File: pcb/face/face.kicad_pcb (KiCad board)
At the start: 2 copper layers, 130 x 65 mm, 25 parts, among them J104 Conn_02x13_Counter_Clockwise, U1 K155ID1, U2 K155ID1, U3 K155ID1, U4 K155ID1

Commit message: Rev B RC1
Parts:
- removed H5: MountingHole, MountingHole:MountingHole_3.2mm_M3_ISO7380
- added H4: MountingHole, MountingHole:MountingHole_3.2mm_M3_ISO7380, F.Cu at (210.0, 120.0)
- added J2: Phoenix MSTB, Connector_Phoenix_MSTB:PhoenixContact_MSTBVA_2,5_3-G-5,08_1x03_P5.08mm_Vertical, B.Cu at (190.9, 118.3)
- J1: renamed from J104; value Conn_02x13_Counter_Clockwise -> 26 pin IDC
- moved C1 1.00 mm to (136.5, 109.0)
- moved C2 1.00 mm to (110.5, 109.0)
- moved C3 1.00 mm to (196.5, 109.0)
- moved C4 1.00 mm to (170.5, 109.0)
- moved H1 1.00 mm to (90.0, 65.0)
- moved H2 1.00 mm to (90.0, 120.0)
- moved H3 1.00 mm to (210.0, 65.0)
- moved J1 1.00 mm to (165.2, 120.0)
- moved NX1 1.00 mm to (151.0, 74.0)
- moved NX2 1.00 mm to (134.0, 79.0)
- moved NX3 1.00 mm to (108.0, 79.0)
- moved NX4 1.00 mm to (151.0, 84.0)
- moved NX5 1.00 mm to (194.0, 79.0)
- moved NX6 1.00 mm to (168.0, 79.0)
- moved R1 1.00 mm to (156.0, 66.0)
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- renumbered C2 to C1, C1 to C2, C4 to C3, C3 to C4, H2 to H1, H4 to H2, NX5 to NX1, NX1 to NX3, NX6 to NX4, NX4 to NX5, NX3 to NX6, R5 to R1, R1 to R3, R6 to R4, R4 to R5, R3 to R6, U2 to U1, U1 to U2, U4 to U3, U3 to U4
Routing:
- net GND: track 0.00 -> 135.3 mm
- net +5V: track 138.5 -> 121.9 mm
- net /NX3_{8}: track 48.6 -> 43.2 mm
- net +170V: track 304.5 -> 306.7 mm
- net M1_{B}: track 42.6 -> 41.3 mm

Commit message: Final Rev B
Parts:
- added REF**: Symbol_HighVoltage_Triangle_8x7mm_SilkScreen, nixie_clock:Symbol_HighVoltage_Triangle_8x7mm_SilkScreen, F.Cu at (182.0, 119.0)
- added REF**: Symbol_HighVoltage_Triangle_8x7mm_SilkScreen, nixie_clock:Symbol_HighVoltage_Triangle_8x7mm_SilkScreen, B.Cu at (182.0, 119.0)
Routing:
- net GND: track 135.3 -> 0.00 mm

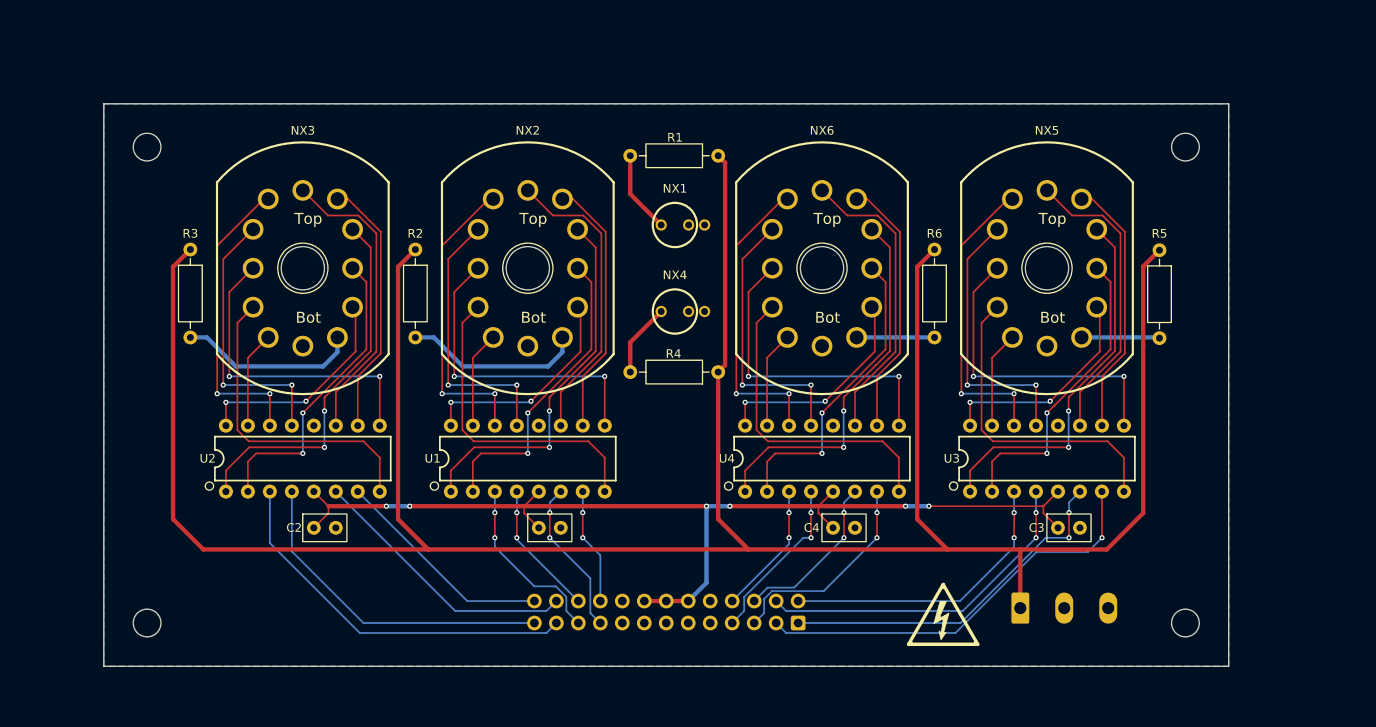
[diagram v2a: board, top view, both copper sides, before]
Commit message: HV converter Rev C redesign around LM5156
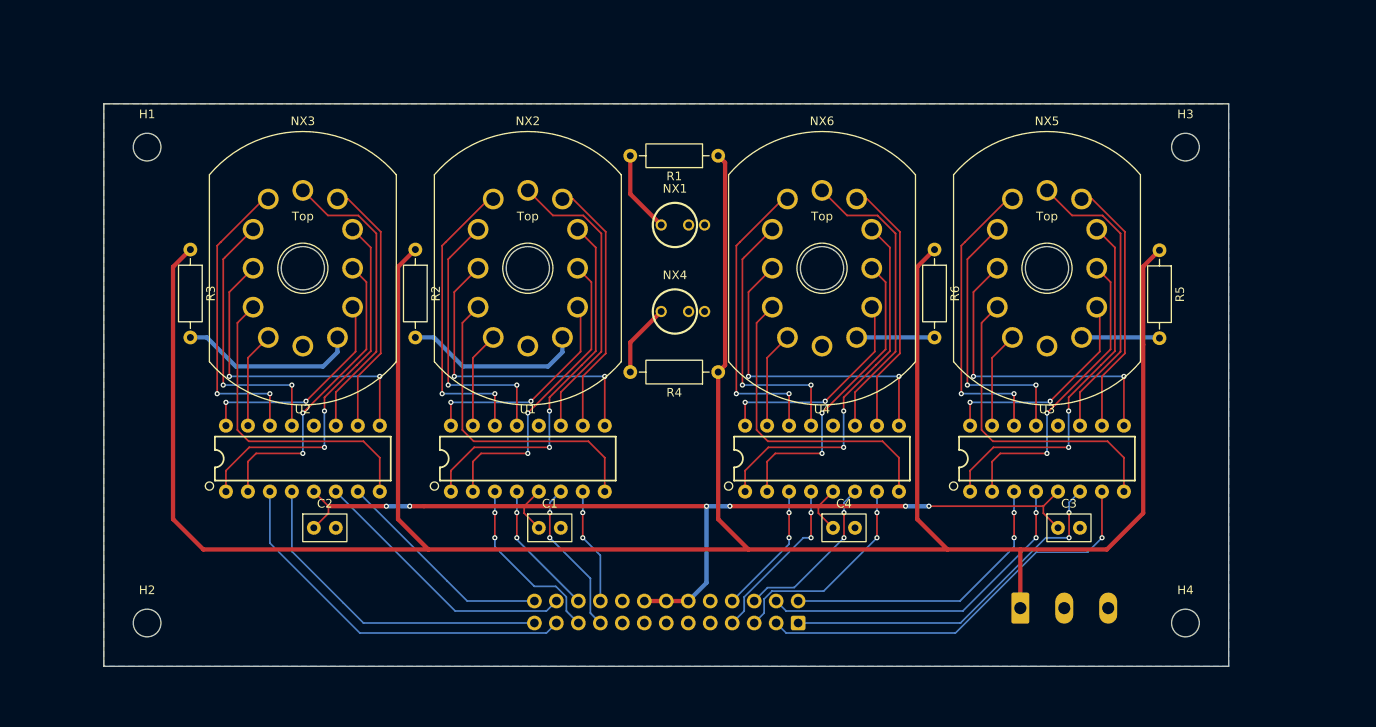
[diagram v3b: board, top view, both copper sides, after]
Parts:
- removed the REF** at (182.0, 119.0) (x2)
- added REF**: Symbol_HighVoltage_Triangle_8x7mm_CopperArrow, 0_nixie_clock:Symbol_HighVoltage_Triangle_8x7mm_CopperArrow, B.Cu at (179.5, 113.5)
- C1, C2, C3, C4: footprint nixie_clock:C_Rect_L5.1mm_W3.2mm_P2.54mm_Goldmax -> 0_nixie_clock:C_Rect_L5.1mm_W3.2mm_P2.54mm_Goldmax
- NX1, NX4: footprint nixie_clock:IN-6 -> 0_nixie_clock:IN-6
- NX2, NX3, NX5, NX6: footprint nixie_clock:IN-12-DSUB -> 0_nixie_clock:IN-12-DSUB
- U1, U2, U3, U4: footprint nixie_clock:DIP16 -> 0_nixie_clock:DIP16

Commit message: Clock Face Rev C
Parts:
- removed the C1 at (136.5, 109.0)
- C3: value 100nF -> 47uF; footprint 0_nixie_clock:C_Rect_L5.1mm_W3.2mm_P2.54mm_Goldmax -> 0_nixie_clock:CP_Radial_D6.3mm_P2.50mm
- moved C3 67.5 mm to (144.5, 66.0), turned to 90 degrees
- moved J1 62.3 mm to (134.2, 66.0)
- moved J2 56.3 mm to (176.0, 64.0)
- moved REF** 52.2 mm to (163.0, 64.0)
- moved C1 35.1 mm to (145.5, 112.0), turned to 90 degrees
- moved C2 17.3 mm to (153.5, 112.0), turned to 90 degrees
- moved R6 13.0 mm to (155.1, 104.0)
- moved NX6 12.0 mm to (150.0, 96.0)
- moved NX1 11.2 mm to (106.0, 90.0)
- moved NX2 11.2 mm to (132.0, 90.0)
- moved U1 11.2 mm to (106.0, 112.0)
- moved U2 11.2 mm to (132.0, 112.0)
- moved NX3 11.0 mm to (168.0, 90.0)
- moved NX4 11.0 mm to (194.0, 90.0)
- moved U3 11.0 mm to (168.0, 112.0)
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- renumbered C2 to C1, C4 to C2, NX3 to NX1, NX6 to NX3, NX5 to NX4, NX1 to NX5, NX4 to NX6, R3 to R1, R6 to R3, R5 to R4, R1 to R5, R4 to R6, U2 to U1, U1 to U2, U4 to U3, U3 to U4
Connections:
- J1 pad 1: M1_{B} -> M1_{A}
- J1 pad 19: H1_{B} -> H10_{A}
- J1 pad 2: M1_{A} -> M10_{C}
- J1 pad 21: H1_{A} -> H10_{D}
- J1 pad 22: H1_{D} -> H1_{B}
- J1 pad 23: H10_{A} -> H10_{B}
- J1 pad 24: H10_{B} -> H1_{D}
- J1 pad 25: H10_{D} -> H10_{C}
- J1 pad 26: H10_{C} -> H1_{A}
- J1 pad 3: M1_{C} -> M1_{D}
- J1 pad 4: M1_{D} -> M10_{B}
- J1 pad 5: M10_{C} -> M1_{B}
- J1 pad 6: M10_{B} -> M10_{D}
- J1 pad 7: M10_{D} -> M1_{C}
- NX1 pad 0: /NX1_{0} -> NX1_{0}
- NX1 pad 1: /NX1_{1} -> NX1_{1}
- NX1 pad 2: /NX1_{2} -> NX1_{2}
- NX1 pad 3: /NX1_{3} -> NX1_{3}
- NX1 pad 4: /NX1_{4} -> NX1_{4}
- NX1 pad 5: /NX1_{5} -> NX1_{5}
- NX1 pad 6: /NX1_{6} -> NX1_{6}
- NX1 pad 7: /NX1_{7} -> NX1_{7}
- NX1 pad 8: /NX1_{8} -> NX1_{8}
- NX1 pad 9: /NX1_{9} -> NX1_{9}
- NX2 pad 0: /NX2_{0} -> NX2_{0}
- NX2 pad 1: /NX2_{1} -> NX2_{1}
- NX2 pad 2: /NX2_{2} -> NX2_{2}
- NX2 pad 3: /NX2_{3} -> NX2_{3}
- NX2 pad 4: /NX2_{4} -> NX2_{4}
- NX2 pad 5: /NX2_{5} -> NX2_{5}
- NX2 pad 6: /NX2_{6} -> NX2_{6}
- NX2 pad 7: /NX2_{7} -> NX2_{7}
- NX2 pad 8: /NX2_{8} -> NX2_{8}
- NX2 pad 9: /NX2_{9} -> NX2_{9}
- NX3 pad 0: /NX3_{0} -> NX3_{0}
- NX3 pad 1: /NX3_{1} -> NX3_{1}
- NX3 pad 2: /NX3_{2} -> NX3_{2}
- NX3 pad 3: /NX3_{3} -> NX3_{3}
- NX3 pad 4: /NX3_{4} -> NX3_{4}
- NX3 pad 5: /NX3_{5} -> NX3_{5}
- NX3 pad 6: /NX3_{6} -> NX3_{6}
- NX3 pad 7: /NX3_{7} -> NX3_{7}
- NX3 pad 8: /NX3_{8} -> NX3_{8}
- NX3 pad 9: /NX3_{9} -> NX3_{9}
- NX4 pad 0: /NX4_{0} -> NX4_{0}
- NX4 pad 1: /NX4_{1} -> NX4_{1}
- NX4 pad 2: /NX4_{2} -> NX4_{2}
- NX4 pad 3: /NX4_{3} -> NX4_{3}
- NX4 pad 4: /NX4_{4} -> NX4_{4}
- NX4 pad 5: /NX4_{5} -> NX4_{5}
- NX4 pad 6: /NX4_{6} -> NX4_{6}
- NX4 pad 7: /NX4_{7} -> NX4_{7}
- NX4 pad 8: /NX4_{8} -> NX4_{8}
- NX4 pad 9: /NX4_{9} -> NX4_{9}
- U1 pad 1: /NX1_{8} -> NX1_{6}
- U1 pad 10: /NX1_{7} -> NX1_{9}
- U1 pad 11: /NX1_{6} -> NX1_{0}
- U1 pad 13: /NX1_{4} -> NX1_{1}
- U1 pad 14: /NX1_{5} -> NX1_{2}
- U1 pad 15: /NX1_{1} -> NX1_{3}
- U1 pad 16: /NX1_{0} -> NX1_{4}
- U1 pad 2: /NX1_{9} -> NX1_{5}
- U1 pad 8: /NX1_{2} -> NX1_{7}
- U1 pad 9: /NX1_{3} -> NX1_{8}
- U2 pad 1: /NX2_{8} -> NX2_{6}
- U2 pad 10: /NX2_{7} -> NX2_{9}
- U2 pad 11: /NX2_{6} -> NX2_{0}
- U2 pad 13: /NX2_{4} -> NX2_{1}
- U2 pad 14: /NX2_{5} -> NX2_{2}
- U2 pad 15: /NX2_{1} -> NX2_{3}
- U2 pad 16: /NX2_{0} -> NX2_{4}
- U2 pad 2: /NX2_{9} -> NX2_{5}
- U2 pad 8: /NX2_{2} -> NX2_{7}
- U2 pad 9: /NX2_{3} -> NX2_{8}
- U3 pad 1: /NX3_{8} -> NX3_{6}
- U3 pad 10: /NX3_{7} -> NX3_{9}
- U3 pad 11: /NX3_{6} -> NX3_{0}
- U3 pad 13: /NX3_{4} -> NX3_{1}
- U3 pad 14: /NX3_{5} -> NX3_{2}
- U3 pad 15: /NX3_{1} -> NX3_{3}
- U3 pad 16: /NX3_{0} -> NX3_{4}
- U3 pad 2: /NX3_{9} -> NX3_{5}
- U3 pad 8: /NX3_{2} -> NX3_{7}
- U3 pad 9: /NX3_{3} -> NX3_{8}
- U4 pad 1: /NX4_{8} -> NX4_{6}
- U4 pad 10: /NX4_{7} -> NX4_{9}
- U4 pad 11: /NX4_{6} -> NX4_{0}
- U4 pad 13: /NX4_{4} -> NX4_{1}
- U4 pad 14: /NX4_{5} -> NX4_{2}
- U4 pad 15: /NX4_{1} -> NX4_{3}
- U4 pad 16: /NX4_{0} -> NX4_{4}
- U4 pad 2: /NX4_{9} -> NX4_{5}
- U4 pad 8: /NX4_{2} -> NX4_{7}
- U4 pad 9: /NX4_{3} -> NX4_{8}
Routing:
- net M10_{A}: track 15.4 -> 186.6 mm, vias 2 -> 0
- net M10_{D}: track 19.5 -> 179.2 mm, vias 2 -> 0
- net +170V: track 306.7 -> 154.7 mm
- net M10_{B}: track 19.3 -> 169.3 mm, vias 2 -> 0
- net M10_{C}: track 24.6 -> 161.4 mm, vias 2 -> 0
- net H1_{C}: track 13.5 -> 126.5 mm, vias 2 -> 0
- net M1_{A}: track 33.9 -> 142.7 mm, vias 2 -> 0
- net M1_{D}: track 39.4 -> 140.6 mm, vias 2 -> 0
- net H1_{B}: track 18.1 -> 119.2 mm, vias 2 -> 0
- net M1_{B}: track 41.3 -> 136.2 mm, vias 2 -> 0
- net H1_{D}: track 15.6 -> 109.3 mm, vias 2 -> 0
- net M1_{C}: track 48.0 -> 134.4 mm, vias 1 -> 0
- net H1_{A}: track 20.6 -> 101.3 mm, vias 2 -> 0
- net +5V: track 121.9 -> 189.7 mm, vias 6 -> 3
- net H10_{C}: track 25.6 -> 82.6 mm
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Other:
- board size 130 x 65 mm -> 140 x 70 mm
